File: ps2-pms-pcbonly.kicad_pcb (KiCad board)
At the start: 2 copper layers, 54.7 x 47 mm, 106 parts, among them U1 SC174, U2 ADP151, U3 BQ24076, U4 TPS61253

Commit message: fix(ps2-pms-pcbonly): fixed clearance errors
BREAKING CHANGE:
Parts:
- removed ? (x5): , 
- removed BLED, Cathode, RLED: TestPoint_Pad_1.0x1.0mm, TestPoint:TestPoint_Pad_1.0x1.0mm
- removed the C9 at (231.1, 127.6)
- removed the C9 at (184.8, 113.5)
- removed the R11 at (237.0, 122.2)
- removed the R11 at (229.9, 119.6)
- removed the R11 at (179.7, 97.7)
- removed the R11 at (176.8, 114.6)
- removed the R11 at (246.9, 122.5)
- removed the R11 at (179.4, 107.5)
- removed the REF** at (181.4, 109.7)
- removed the REF** at (181.5, 115.4)
- removed the REF** at (229.2, 124.2)
- removed the REF** at (178.4, 104.0)
- removed the REF** at (185.2, 86.7)
- removed the REF** at (240.5, 121.2)
- removed the REF** at (234.9, 124.2)
- added 5-pin: 5pin FPC, ps2+:5pin FPC, F.Cu at (16.2, 49.9)
- added BC846: BC846A, ps2-pms:BC846A, B.Cu at (44.2, 39.9)
- added BC846: BC846A, ps2-pms:BC846A, B.Cu at (28.8, 51.9)
- added C16: C_0805_2012Metric, Capacitor_SMD:C_0805_2012Metric, B.Cu at (27.9, 54.9)
- added R17: R_0603_1608Metric, Resistor_SMD:R_0603_1608Metric, B.Cu at (46.8, 35.9)
- added R18: R_0603_1608Metric, Resistor_SMD:R_0603_1608Metric, B.Cu at (47.4, 40.9)
- added R19: R_0603_1608Metric, Resistor_SMD:R_0603_1608Metric, B.Cu at (31.6, 48.9)
- added R20: R_0603_1608Metric, Resistor_SMD:R_0603_1608Metric, B.Cu at (36.2, 53.9)
- added REF**: TestPoint_Plated_Hole_D2.0mm, TestPoint:TestPoint_Plated_Hole_D2.0mm, F.Cu at (65.7, 57.7)
- added REF**: TestPoint_Plated_Hole_D2.0mm, TestPoint:TestPoint_Plated_Hole_D2.0mm, F.Cu at (65.7, 14.4)
- added REF**: TestPoint_Plated_Hole_D2.0mm, TestPoint:TestPoint_Plated_Hole_D2.0mm, F.Cu at (14.7, 57.7)
- added REF**: TestPoint_Plated_Hole_D2.0mm, TestPoint:TestPoint_Plated_Hole_D2.0mm, F.Cu at (14.7, 14.4)
- added U5: CSD22202W15, ucb-c adapter:CSD22202W15, B.Cu at (45.4, 32.6)
- L1: value inductor-2uh -> Inductor-1uH; footprint ps2-pms:inductor-2uh -> ps2-pms:Inductor-1uH
- moved 5V+ 127.4 mm to (24.7, 56.7)
- moved BAT+ 126.1 mm to (41.3, 56.7)
- moved 1V8+ 126.1 mm to (49.0, 56.7)
- moved 2V5+ 126.1 mm to (53.1, 56.7)
- moved 5V+IN 126.1 mm to (37.3, 56.6)
- moved BAT- 126.1 mm to (45.0, 56.7)
- moved C10 125.6 mm to (57.5, 21.0)
- moved C10 125.6 mm to (59.4, 48.8)
- moved C11 125.6 mm to (52.2, 18.0)
- moved C13 125.6 mm to (54.4, 53.5)
- moved C2 125.6 mm to (26.2, 32.9)
- moved C8 125.6 mm to (53.0, 34.8)
- moved R8 125.6 mm to (39.5, 42.7)
- moved U1 125.6 mm to (46.0, 23.1)
- moved BC847C 125.6 mm to (25.6, 44.2)
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- renumbered R14 to R21, R14 to R22
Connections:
- U3 pad 15: GND -> SYSOFF
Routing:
- net sysoff: track 83.8 -> 0.00 mm, vias 4 -> 0
- net BTN+: track 0.00 -> 48.1 mm, vias 0 -> 1
- net BTN-: track 0.00 -> 47.9 mm, vias 0 -> 1
- net source: track 45.0 -> 0.00 mm, vias 7 -> 0
- net SYSOFF: track 0.00 -> 41.0 mm, vias 0 -> 1
- net BAT+: track 73.3 -> 107.4 mm
- net RLED: track 33.1 -> 9.93 mm
- net SOURCE: track 0.00 -> 17.2 mm, vias 0 -> 1
- net Cathode: track 48.4 -> 40.3 mm
- net GND: track 21.9 -> 17.3 mm, vias 32 -> 29
- net (no net): track 4.06 -> 0.00 mm, vias 2 -> 0
- net 3V8+: track 153.8 -> 156.6 mm
- net Anode: track 44.2 -> 41.7 mm
- net SW: track 14.4 -> 12.7 mm
- net 2V5+: track 34.5 -> 33.1 mm
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
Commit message: feat(gerber-files): added ready files for pcb websites
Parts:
- added G***: LOGO, graphics:iblis 5mm, B.Cu at (17.1, 43.2)
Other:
- board text added: "Made by DDIBLIS"
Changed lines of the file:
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@@
       (outputformat 1)
       (mirror false)
-      (drillshape 1)
+      (drillshape 0)
       (scaleselection 1)
-      (outputdirectory "")
+      (outputdirectory "Gerber-files/")
     )
   )
@@
     )
   )
+  (footprint "graphics:iblis 5mm" (layer "B.Cu")
+    (at 17.1 43.2 180)
+    (attr board_only exclude_from_pos_files exclude_from_bom)
+    (fp_text reference "G***" (at 16.7 9.3) (layer "B.SilkS")
+      (effects (font (size 1.524 1.524) (thickness 0.3)) (justify mirror))
+    )
+    (fp_text value "LOGO" (at 0.75 0) (layer "B.SilkS") hide
+      (effects (font (size 1.524 1.524) (thickness 0.3)) (justify mirror))
+    )
+    (fp_poly (pts
+        (xy 1.448886 2.495635)
+        (xy 1.576374 2.481153)
+        (xy 1.686933 2.455416)
+        (xy 1.697135 2.451924)
+        (xy 1.901928 2.343669)
+        (xy 2.091129 2.175482)
+        (xy 2.256082 1.957545)
+        (xy 2.388129 1.700041)
+        (xy 2.428795 1.591221)
+        (xy 2.475747 1.389618)
+        (xy 2.500255 1.147213)
+        (xy 2.502157 0.890045)
+        (xy 2.48129 0.644154)
+        (xy 2.437488 0.435581)
+        (xy 2.436083 0.431022)
+        (xy 2.339766 0.200421)
+        (xy 2.201075 -0.028867)
+        (xy 2.038224 -0.228746)
+        (xy 1.960295 -0.303008)
+        (xy 1.837777 -0.396775)
+        (xy 1.700576 -0.483411)
+        (xy 1.568195 -0.552257)
+        (xy 1.460139 -0.592656)
+        (xy 1.418838 -0.59889)
+        (xy 1.359247 -0.58028)
+        (xy 1.262603 -0.531388)
+        (xy 1.149376 -0.462619)
+        (xy 1.144643 -0.459504)
+        (xy 1.007552 -0.363292)
+        (xy 0.867252 -0.255903)
+        (xy 0.775034 -0.17876)
+        (xy 0.616505 -0.037402)
+        (xy 0.775034 0.095025)
+        (xy 1.030769 0.330706)
+        (xy 1.223149 0.562193)
+        (xy 1.357525 0.800897)
+        (xy 1.439252 1.058227)
+        (xy 1.473681 1.345592)
+        (xy 1.472037 1.580644)
+        (xy 1.45199 1.805519)
+        (xy 1.41116 1.986991)
+        (xy 1.341068 2.151033)
+        (xy 1.233234 2.323616)
+        (xy 1.226181 2.333671)
+        (xy 1.185752 2.40895)
+        (xy 1.178538 2.46278)
+        (xy 1.180018 2.465779)
+        (xy 1.22919 2.488524)
+        (xy 1.325985 2.498284)
+      ) (layer "B.SilkS") (width 0) (fill solid))
+    (fp_poly (pts
+        (xy -1.237894 2.490223)
+        (xy -1.182432 2.468934)
+        (xy -1.180018 2.465779)
+        (xy -1.183401 2.415678)
+        (xy -1.221031 2.341177)
+        (xy -1.226182 2.333671)
+        (xy -1.329798 2.17292)
+        (xy -1.399242 2.024643)
+        (xy -1.441854 1.865411)
+        (xy -1.464975 1.671797)
+        (xy -1.471719 1.55007)
+        (xy -1.476778 1.365434)
+        (xy -1.472369 1.227708)
+        (xy -1.456142 1.113703)
+        (xy -1.425747 1.000231)
+        (xy -1.411619 0.957214)
+        (xy -1.321431 0.735154)
+        (xy -1.205803 0.538927)
+        (xy -1.052844 0.352426)
+        (xy -0.850664 0.159549)
+        (xy -0.775035 0.095024)
+        (xy -0.616505 -0.037402)
+        (xy -0.775035 -0.17876)
+        (xy -0.902043 -0.284297)
+        (xy -1.041772 -0.388103)
+        (xy -1.179473 -0.480556)
+        (xy -1.300396 -0.552035)
+        (xy -1.38979 -0.592917)
+        (xy -1.419071 -0.59889)
+        (xy -1.488937 -0.583418)
+        (xy -1.586882 -0.544733)
+        (xy -1.620185 -0.528607)
+        (xy -1.757952 -0.458324)
+        (xy -1.817773 -0.648096)
+        (xy -1.847524 -0.761753)
+        (xy -1.860661 -0.853048)
+        (xy -1.85774 -0.889604)
+        (xy -1.809975 -0.927265)
+        (xy -1.709604 -0.954778)
+        (xy -1.671045 -0.960146)
+        (xy -1.555617 -0.986268)
+        (xy -1.409829 -1.037174)
+        (xy -1.264175 -1.102132)
+        (xy -1.256649 -1.105963)
+        (xy -1.009096 -1.232975)
+        (xy -0.724728 -1.095017)
+        (xy -0.509312 -0.984816)
+        (xy -0.347347 -0.886031)
+        (xy -0.225535 -0.78752)
+        (xy -0.130578 -0.678144)
+        (xy -0.049177 -0.546762)
+        (xy -0.032395 -0.515012)
+        (xy 0.03637 -0.390109)
+        (xy 0.091351 -0.315526)
+        (xy 0.145926 -0.276571)
+        (xy 0.198856 -0.26108)
+        (xy 0.333013 -0.262702)
+        (xy 0.428851 -0.316212)
+        (xy 0.477309 -0.409405)
+        (xy 0.469329 -0.530073)
+        (xy 0.444151 -0.59156)
+        (xy 0.343458 -0.726598)
+        (xy 0.183372 -0.866068)
+        (xy -0.02588 -1.003595)
+        (xy -0.274068 -1.132802)
+        (xy -0.550963 -1.247314)
+        (xy -0.677901 -1.290963)
+        (xy -0.809473 -1.343583)
+        (xy -0.874261 -1.394232)
+        (xy -0.87085 -1.441483)
+        (xy -0.846914 -1.461118)
+        (xy -0.818172 -1.504175)
+        (xy -0.78045 -1.592493)
+        (xy -0.755146 -1.665887)
+        (xy -0.72156 -1.795696)
+        (xy -0.717375 -1.89854)
+        (xy -0.736601 -1.996142)
+        (xy -0.812017 -2.153444)
+        (xy -0.938513 -2.288456)
+        (xy -1.100905 -2.395113)
+        (xy -1.284006 -2.467345)
+        (xy -1.472633 -2.499087)
+        (xy -1.651598 -2.48427)
+        (xy -1.799756 -2.420926)
+        (xy -1.929399 -2.301168)
+        (xy -1.995806 -2.155294)
+        (xy -2.005231 -2.066591)
+        (xy -1.8319 -2.066591)
+        (xy -1.800196 -2.205728)
+        (xy -1.712939 -2.313609)
+        (xy -1.581914 -2.379718)
+        (xy -1.463304 -2.395561)
+        (xy -1.319285 -2.37811)
+        (xy -1.181498 -2.334297)
+        (xy -1.16558 -2.326649)
+        (xy -0.994165 -2.209252)
+        (xy -0.88745 -2.067532)
+        (xy -0.846885 -1.906074)
+        (xy -0.873919 -1.729462)
+        (xy -0.93505 -1.5972)
+        (xy -0.993433 -1.50933)
+        (xy -1.043391 -1.454078)
+        (xy -1.062227 -1.444383)
+        (xy -1.12739 -1.463504)
+        (xy -1.231968 -1.514033)
+        (xy -1.358553 -1.585711)
+        (xy -1.489738 -1.668282)
+        (xy -1.608118 -1.751491)
+        (xy -1.674933 -1.805406)
+        (xy -1.768029 -1.895274)
+        (xy -1.81579 -1.967992)
+        (xy -1.831449 -2.045578)
+        (xy -1.8319 -2.066591)
+        (xy -2.005231 -2.066591)
+        (xy -2.007525 -2.045001)
+        (xy -1.999791 -1.974677)
+        (xy -1.968972 -1.907528)
+        (xy -1.90464 -1.827259)
+        (xy -1.800496 -1.721594)
+        (xy -1.670247 -1.605867)
+        (xy -1.525501 -1.493829)
+        (xy -1.396849 -1.409104)
+        (xy -1.392924 -1.406873)
+        (xy -1.192899 -1.293986)
+        (xy -1.29222 -1.227803)
+        (xy -1.392588 -1.175353)
+        (xy -1.526267 -1.123162)
+        (xy -1.664267 -1.080929)
+        (xy -1.7776 -1.058355)
+        (xy -1.803066 -1.056865)
+        (xy -1.841854 -1.068399)
+        (xy -1.861163 -1.114075)
+        (xy -1.867033 -1.210502)
+        (xy -1.867129 -1.233009)
+        (xy -1.870831 -1.333518)
+        (xy -1.880293 -1.397292)
+        (xy -1.887694 -1.409154)
+        (xy -1.927713 -1.387099)
+        (xy -2.004702 -1.329205)
+        (xy -2.104277 -1.247875)
+        (xy -2.212059 -1.155512)
+        (xy -2.313666 -1.064521)
+        (xy -2.394715 -0.987305)
+        (xy -2.440827 -0.936268)
+        (xy -2.445717 -0.927867)
+        (xy -2.43435 -0.864193)
+        (xy -2.365985 -0.782609)
+        (xy -2.24932 -0.690669)
+        (xy -2.093051 -0.595927)
+        (xy -2.020319 -0.558404)
+        (xy -1.791753 -0.445881)
+        (xy -1.949029 -0.311445)
+        (xy -2.129826 -0.122592)
+        (xy -2.289297 0.108372)
+        (xy -2.408885 0.353158)
+        (xy -2.436084 0.431022)
+        (xy -2.480467 0.638316)
+        (xy -2.501911 0.883585)
+        (xy -2.500583 1.140789)
+        (xy -2.476643 1.383887)
+        (xy -2.430257 1.586841)
+        (xy -2.428796 1.591221)
+        (xy -2.311908 1.861382)
+        (xy -2.158744 2.095942)
+        (xy -1.97796 2.284719)
+        (xy -1.778211 2.417531)
+        (xy -1.697135 2.451924)
+        (xy -1.589751 2.478864)
+        (xy -1.463072 2.494611)
+        (xy -1.338613 2.49859)
+      ) (layer "B.SilkS") (width 0) (fill solid))
+  )
   (footprint "Capacitor_SMD:C_1206_3216Metric" (layer "B.Cu")
     (at 22.121522 25.383478 90)
@@
   (gr_line (start 67.53 12.565978) (end 67.53 59.540978) (layer "Edge.Cuts") (width 0.15))
   (gr_line (start 12.855 59.540978) (end 12.855 12.565978) (layer "Edge.Cuts") (width 0.15))
+  (gr_text "Made by DDIBLIS\n" (at 57.3 58.1) (layer "B.SilkS")
+    (effects (font (size 1 1) (thickness 0.15)) (justify mirror))
+  )
   (gr_text "+\n" (at 43.66 45.9275) (layer "F.SilkS")
     (effects (font (size 1.5 1.5) (thickness 0.3)))

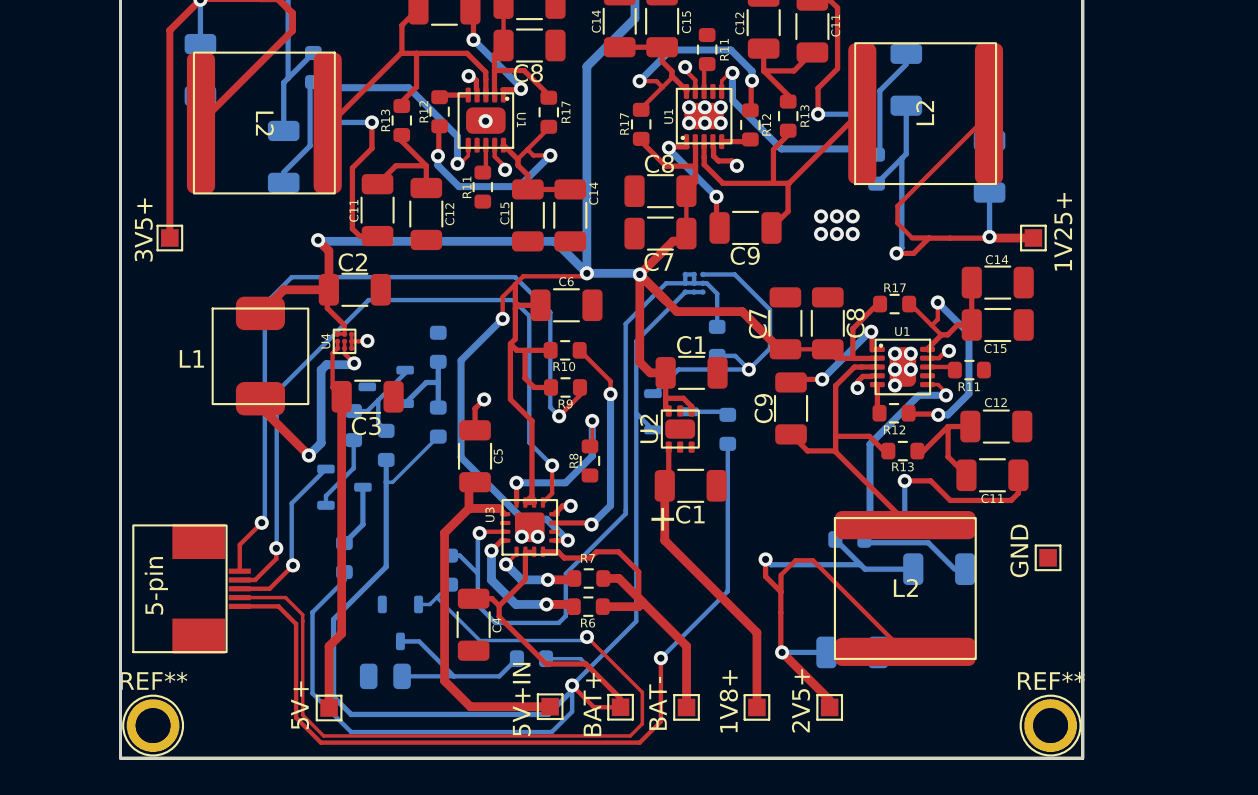
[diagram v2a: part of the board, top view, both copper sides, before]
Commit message: docs(added-BOM): Added Bill of materials
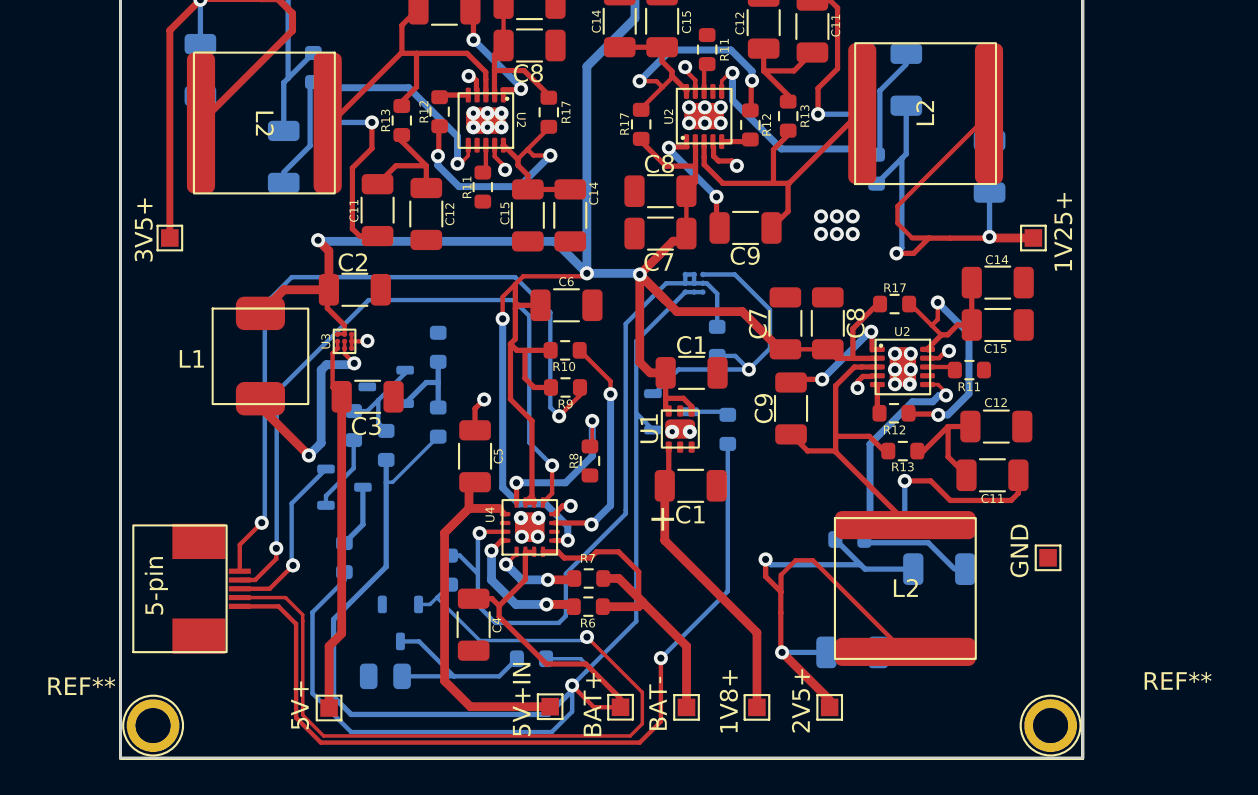
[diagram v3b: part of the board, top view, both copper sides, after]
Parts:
- renumbered U2 to U1, U1 to U2, U4 to U3, U3 to U4
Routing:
- net 3V8+: track 156.6 -> 154.7 mm
- net GND: vias 29 -> 39
